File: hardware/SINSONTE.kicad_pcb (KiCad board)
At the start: 2 copper layers, 90 x 70 mm, 20 parts, among them J1 BAT, J2 CLOCK, J3 LIGHT_SENSOR, J4 Conn_01x17_Male, Q1 2N7000, Q2 PN2222A, SW1 SW_Push, U1 Pico

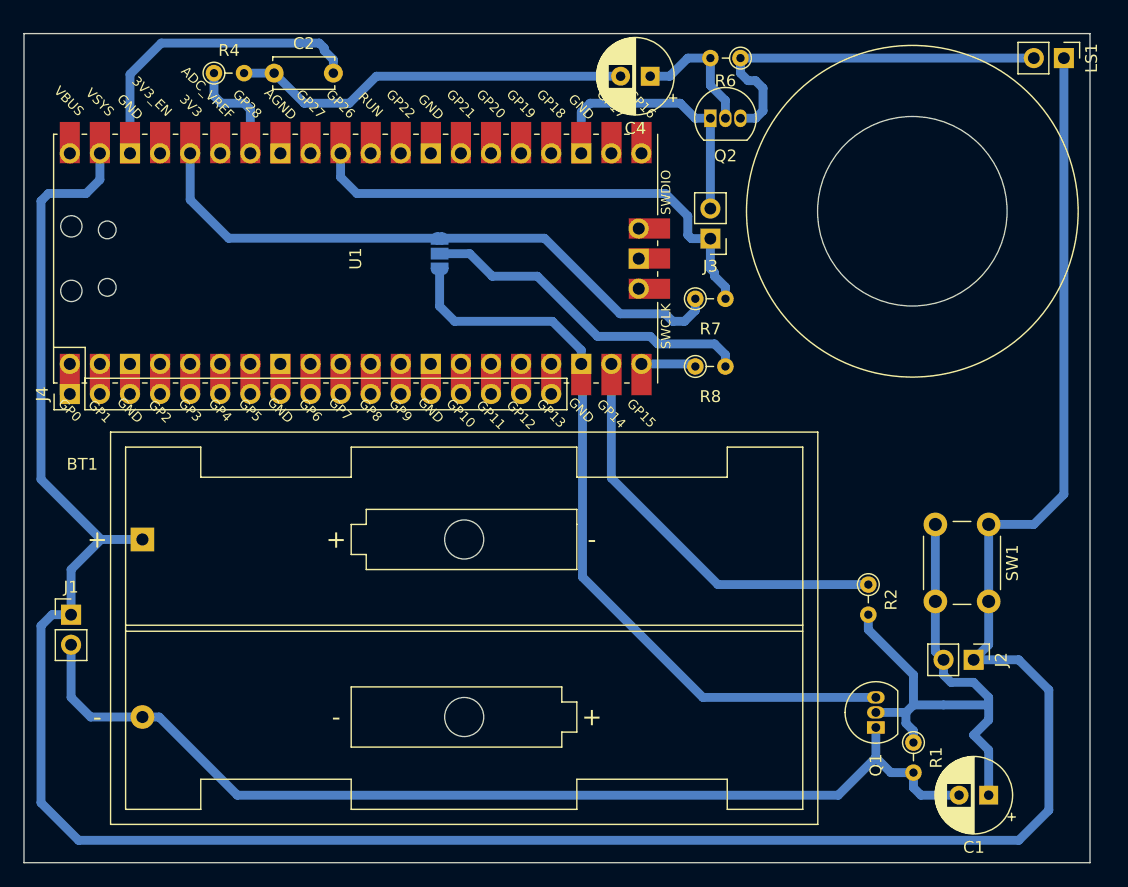
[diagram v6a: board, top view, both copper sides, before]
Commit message: changed autopower off strategy
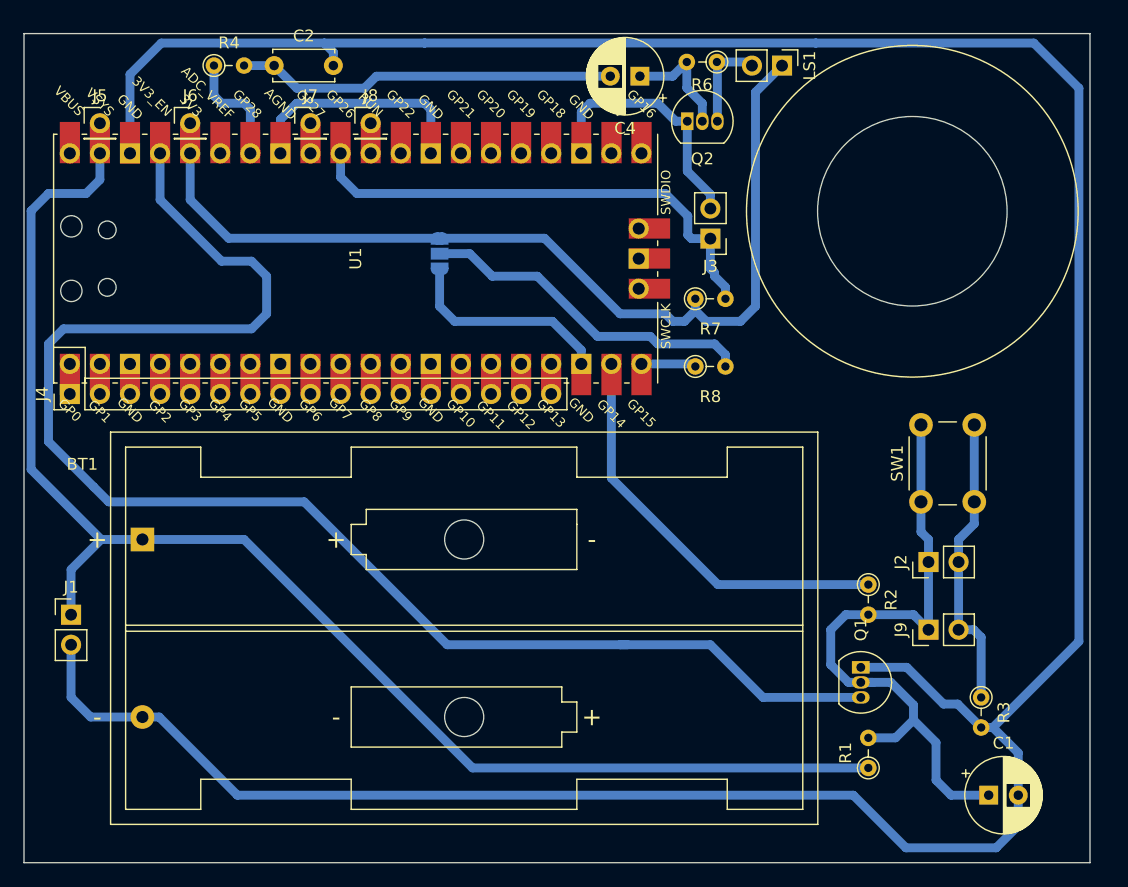
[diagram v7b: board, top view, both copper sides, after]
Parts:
- added J5: Conn_01x01_Male, Connector_PinHeader_2.54mm:PinHeader_1x01_P2.54mm_Vertical, F.Cu at (56.4, 57.6)
- added J6: Conn_01x01_Male, Connector_PinHeader_2.54mm:PinHeader_1x01_P2.54mm_Vertical, F.Cu at (64.0, 57.6)
- added J7: Conn_01x01_Male, Connector_PinHeader_2.54mm:PinHeader_1x01_P2.54mm_Vertical, F.Cu at (74.2, 57.6)
- added J8: Conn_01x01_Male, Connector_PinHeader_2.54mm:PinHeader_1x01_P2.54mm_Vertical, F.Cu at (79.3, 57.6)
- added J9: PROG, Connector_PinHeader_2.54mm:PinHeader_1x02_P2.54mm_Vertical, F.Cu at (126.4, 100.3)
- added R3: R, Resistor_THT:R_Axial_DIN0204_L3.6mm_D1.6mm_P2.54mm_Vertical, F.Cu at (130.8, 106.0)
- moved LS1 23.8 mm to (114.0, 52.7)
- moved J2 9.09 mm to (126.4, 94.6), turned to 90 degrees
- moved SW1 6.02 mm to (125.7, 89.5), turned to 90 degrees
- moved Q1 5.24 mm to (120.7, 103.5), turned to 270 degrees
- moved R1 4.37 mm to (121.3, 112.0), turned to 90 degrees
- moved R6 2.02 mm to (108.5, 52.4)
- moved Q2 1.97 mm to (106.0, 57.4)
- moved C4 0.87 mm to (102.0, 53.6)
- moved C2 0.64 mm to (71.1, 52.7)
- moved R4 0.64 mm to (66.0, 52.7)
- turned C1 to 0 degrees
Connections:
- C2 pad 2: Net-(C2-Pad2) -> Net-(BT1-Pad2)
- J2 pad 1: Net-(BT1-Pad1) -> Net-(C1-Pad1)
- J2 pad 2: Net-(C1-Pad1) -> Net-(J2-Pad2)
- JP1 pad 1: Net-(JP1-Pad1) -> Net-(J6-Pad1)
- LS1 pad 1: Net-(BT1-Pad1) -> Net-(J6-Pad1)
- Q1 pad 3: Net-(JP1-Pad3) -> Net-(Q1-Pad3)
- R1 pad 1: Net-(C1-Pad1) -> Net-(BT1-Pad1)
- R1 pad 2: Net-(BT1-Pad2) -> Net-(C1-Pad1)
- R7 pad 1: Net-(JP1-Pad1) -> Net-(J6-Pad1)
- SW1 pad 1: Net-(BT1-Pad1) -> Net-(C1-Pad1)
- SW1 pad 2: Net-(C1-Pad1) -> Net-(J2-Pad2)
- U1 pad 33: Net-(U1-Pad33) -> Net-(U1-Pad28)
- U1 pad 36: Net-(JP1-Pad1) -> Net-(J6-Pad1)
- U1 pad 37: Net-(U1-Pad37) -> Net-(Q1-Pad3)
- U1 pad 38: Net-(C2-Pad2) -> Net-(BT1-Pad2)
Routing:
- net Net-(BT1-Pad2): track 88.7 -> 261.7 mm
- net Net-(Q1-Pad3): track 0.00 -> 124.6 mm
- net Net-(BT1-Pad1): track 228.6 -> 122.0 mm
- net Net-(J6-Pad1): track 0.00 -> 82.1 mm
- net Net-(JP1-Pad1): track 52.3 -> 0.00 mm
- net Net-(JP1-Pad3): track 66.4 -> 19.5 mm
- net Net-(C2-Pad2): track 26.9 -> 0.00 mm
- net Net-(J2-Pad2): track 0.00 -> 25.1 mm
- net Net-(LS1-Pad2): track 32.5 -> 8.10 mm
- net Net-(U1-Pad28): track 0.00 -> 20.0 mm
- net Net-(C1-Pad1): track 48.7 -> 55.8 mm
- net Net-(J8-Pad1): track 0.00 -> 2.54 mm
- net Net-(J7-Pad1): track 0.00 -> 2.54 mm
- net Net-(C2-Pad1): track 33.8 -> 32.1 mm
- net Net-(C4-Pad1): track 11.3 -> 10.00 mm
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
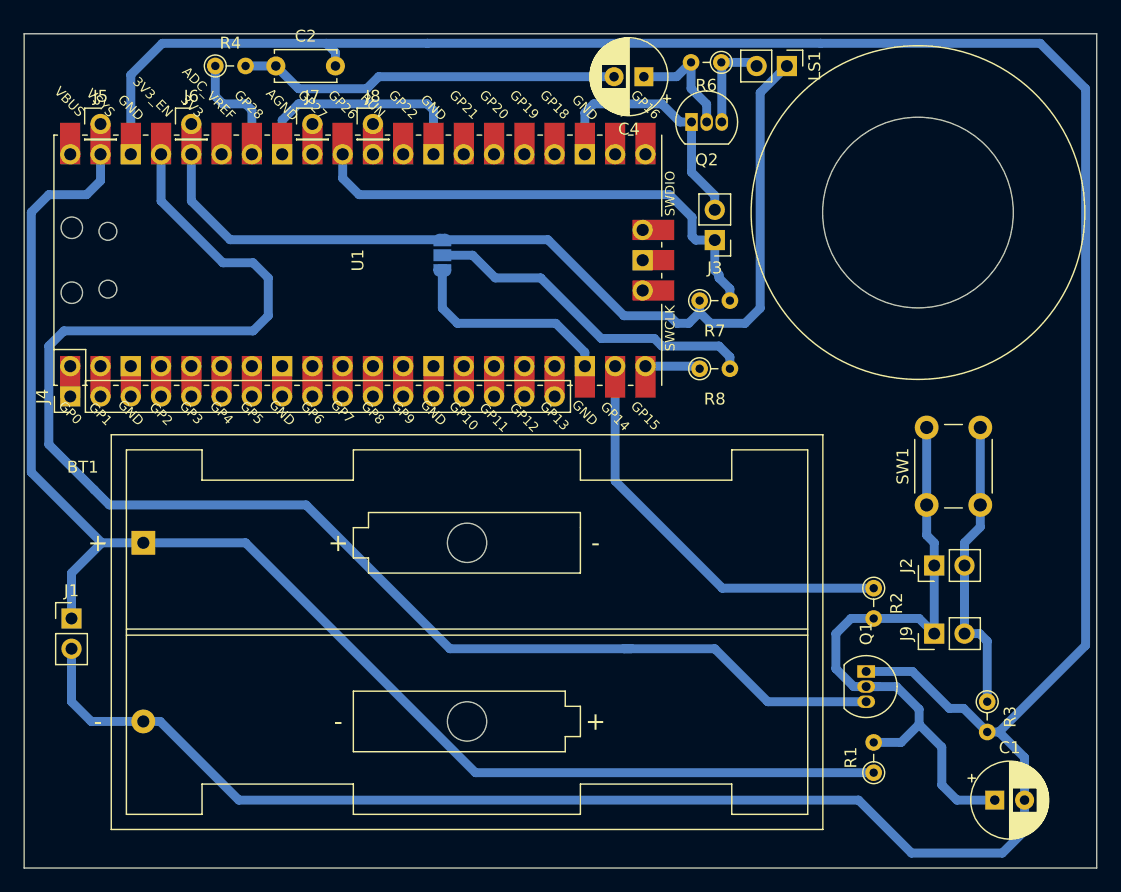
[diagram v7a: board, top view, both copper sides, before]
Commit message: mounting holes
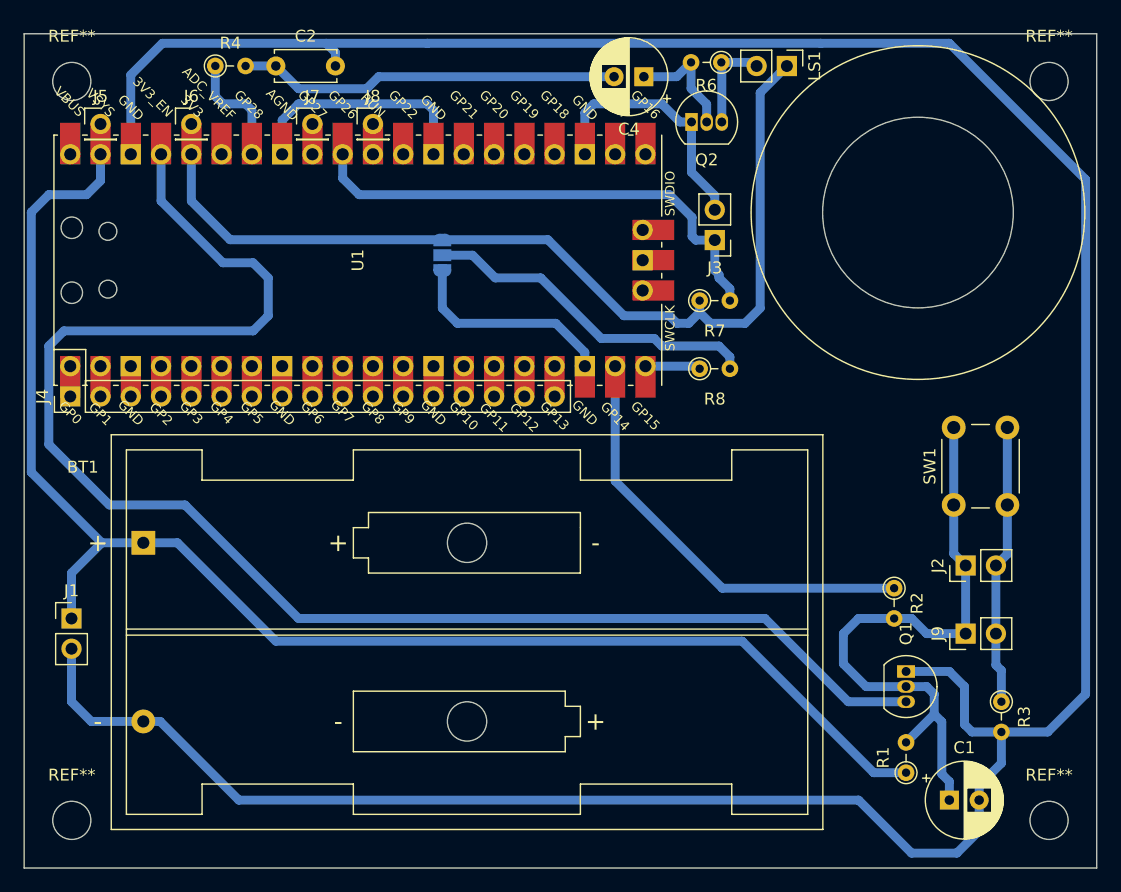
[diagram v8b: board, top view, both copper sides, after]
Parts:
- added REF**: MountingHole_3.2mm_M3_DIN965, MountingHole:MountingHole_3.2mm_M3_DIN965, F.Cu at (54.0, 54.0)
- added REF**: MountingHole_3.2mm_M3_DIN965, MountingHole:MountingHole_3.2mm_M3_DIN965, F.Cu at (136.0, 54.0)
- added REF**: MountingHole_3.2mm_M3_DIN965, MountingHole:MountingHole_3.2mm_M3_DIN965, F.Cu at (136.0, 116.0)
- added REF**: MountingHole_3.2mm_M3_DIN965, MountingHole:MountingHole_3.2mm_M3_DIN965, F.Cu at (54.0, 116.0)
- moved C1 3.81 mm to (127.6, 114.3)
- moved Q1 3.35 mm to (124.0, 103.5)
- moved R1 2.72 mm to (124.0, 112.0)
- moved J2 2.64 mm to (129.0, 94.6)
- moved J9 2.64 mm to (129.0, 100.3)
- moved SW1 2.27 mm to (128.0, 89.5)
- moved R2 1.72 mm to (123.0, 96.5)
- moved R3 1.19 mm to (132.0, 106.0)
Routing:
- net Net-(BT1-Pad2): track 261.7 -> 254.2 mm
- net Net-(C1-Pad1): track 55.8 -> 53.0 mm
- net Net-(BT1-Pad1): track 122.0 -> 124.7 mm
- net Net-(Q1-Pad3): track 124.6 -> 127.4 mm
- net Net-(R2-Pad1): track 35.1 -> 36.8 mm
- net Net-(J2-Pad2): track 25.1 -> 23.6 mm
